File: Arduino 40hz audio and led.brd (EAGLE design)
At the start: 79.2 x 109.7 mm, 37 parts, among them IC1 LM7805, IC2 IRL-Z44N, IC3 LM741

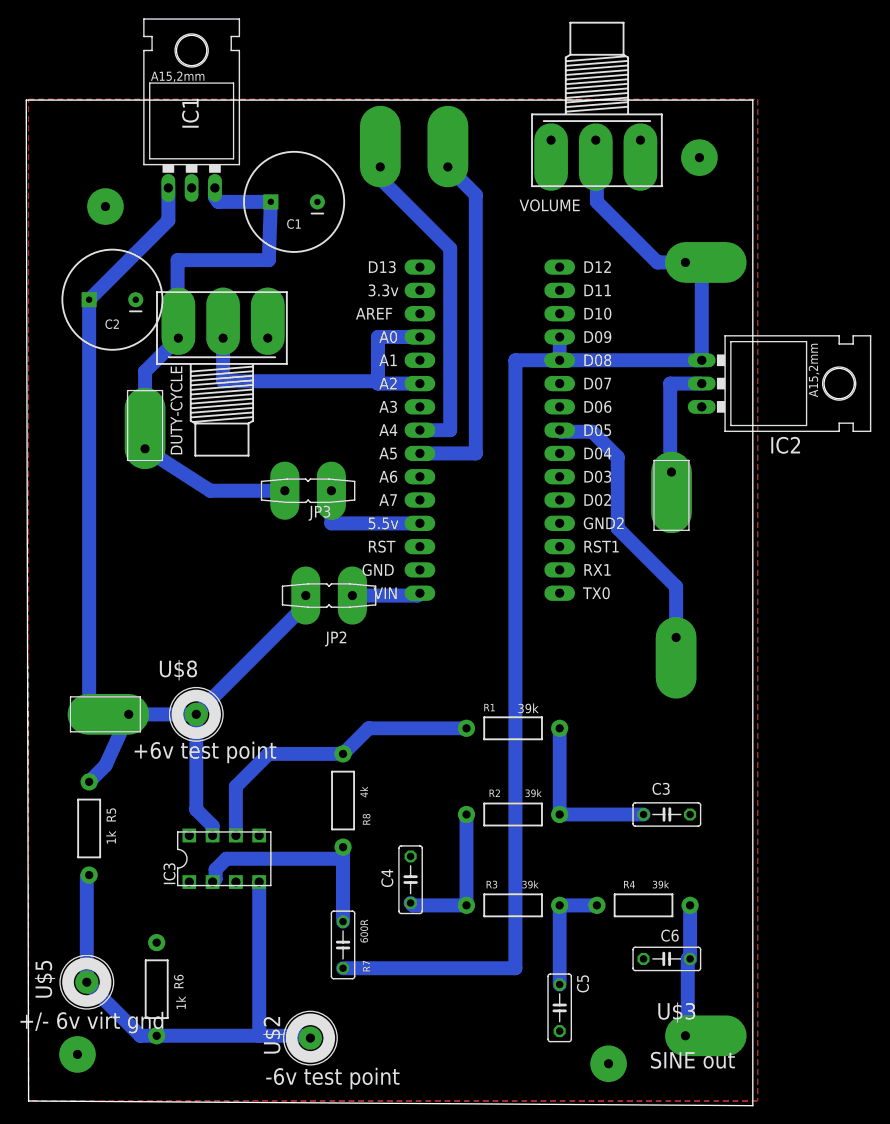
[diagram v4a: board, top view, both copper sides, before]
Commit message: Big update to this branch
Big update to this branch.  This branch I've completed the layout of the
board for single sided copper, where the parts are on top (no copper)
and the traces are on the bottom (copper layer).

I've worked quite a bit at setting trace width, spacing and part
spacing.
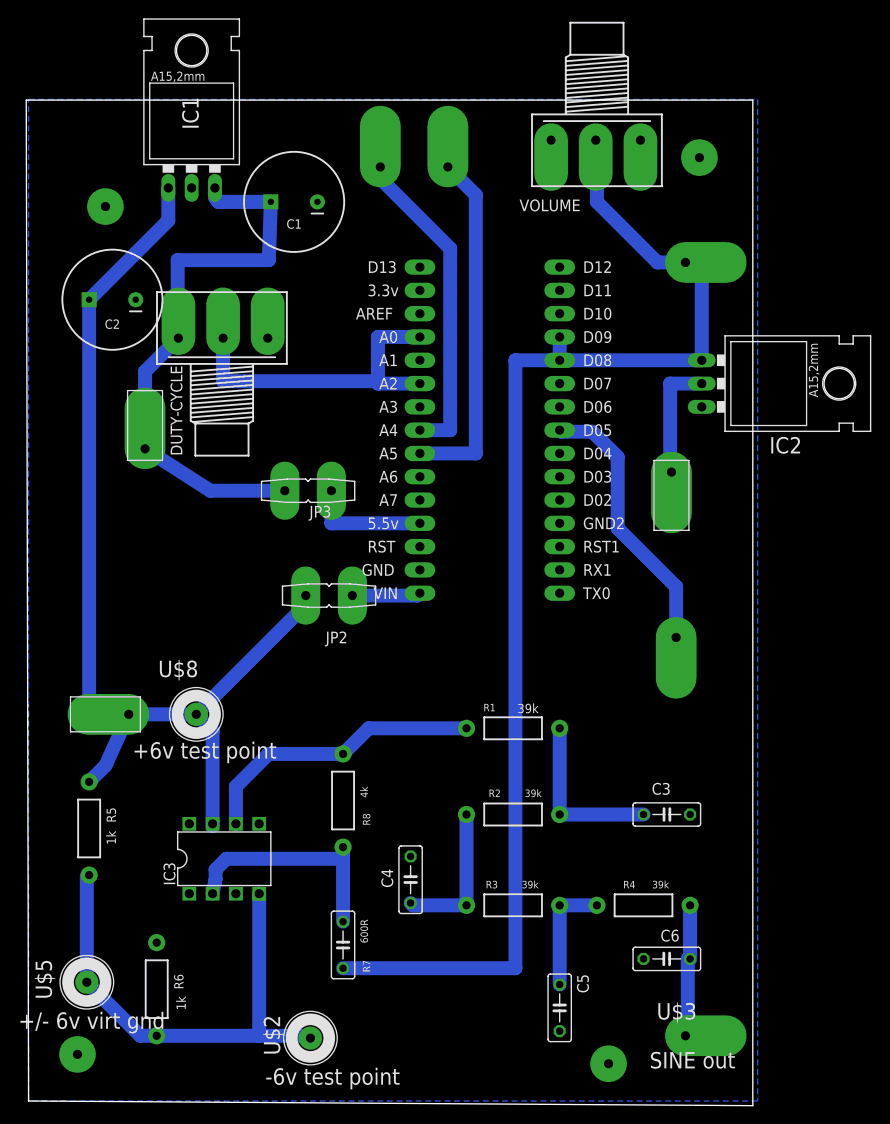
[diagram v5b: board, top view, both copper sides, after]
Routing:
- net N$13: track 33.1 -> 31.8 mm
- net N$12: track 55.5 -> 54.2 mm
- net N$10: track 24.0 -> 25.2 mm
- net +12V: track 113.2 -> 112.1 mm
- added copper zone on layer 16, net GND
- removed copper zone on layer 1, net GND
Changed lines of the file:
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@@
 <?xml version="1.0" encoding="utf-8"?>
 <!DOCTYPE eagle SYSTEM "eagle.dtd">
-<eagle version="9.2.2">
+<eagle version="9.4.2">
 <drawing>
 <settings>
@@
 <contactref element="C4" pad="2"/>
 <contactref element="C5" pad="2"/>
-<polygon width="0.9144" layer="1">
+<polygon width="0.9144" layer="16">
 <vertex x="-0.254" y="0.254"/>
 <vertex x="-0.254" y="109.474"/>
@@
 <wire x1="10.668" y1="42.418" x2="6.35" y2="42.418" width="1.524" layer="16"/>
 <wire x1="6.35" y1="42.418" x2="6.35" y2="87.63" width="1.524" layer="16"/>
-<wire x1="18.034" y1="32.02358125" x2="18.034" y2="42.418" width="1.524" layer="16"/>
-<wire x1="19.812" y1="29.21" x2="19.812" y2="30.24558125" width="1.524" layer="16"/>
-<wire x1="19.812" y1="30.24558125" x2="18.034" y2="32.02358125" width="1.524" layer="16"/>
+<wire x1="19.812" y1="40.64" x2="19.812" y2="30.48" width="1.524" layer="16"/>
+<wire x1="19.812" y1="40.64" x2="18.034" y2="42.418" width="1.524" layer="16"/>
+<wire x1="19.812" y1="30.48" x2="19.812" y2="30.24558125" width="1.524" layer="16"/>
 </signal>
 <signal name="+5V" class="2">
@@
 <wire x1="73.152" y1="78.486" x2="69.7088" y2="78.486" width="1.524" layer="16"/>
 <wire x1="69.7088" y1="78.486" x2="69.7088" y2="67.1972" width="1.524" layer="16"/>
+<wire x1="69.7088" y1="67.1972" x2="69.85" y2="68.834" width="0" layer="19" extent="16-16"/>
 <wire x1="27.686" y1="66.802" x2="69.7088" y2="67.1972" width="0" layer="19" extent="16-16"/>
 </signal>
@@
 <wire x1="20.955" y1="83.439" x2="20.955" y2="78.74" width="1.524" layer="16"/>
 <wire x1="20.955" y1="78.74" x2="37.846" y2="78.74" width="1.524" layer="16"/>
+<wire x1="42.164" y1="78.486" x2="42.418" y2="78.486" width="0" layer="19" extent="16-16"/>
 </signal>
 <signal name="N$2" class="2">
@@
 <wire x1="34.036" y1="38.1" x2="36.83" y2="40.894" width="1.524" layer="16"/>
 <wire x1="36.83" y1="40.894" x2="47.498" y2="40.894" width="1.524" layer="16"/>
-<wire x1="22.352" y1="29.21" x2="22.352" y2="34.544" width="1.524" layer="16"/>
+<wire x1="22.352" y1="30.48" x2="22.352" y2="34.544" width="1.524" layer="16"/>
 <wire x1="22.352" y1="34.544" x2="25.908" y2="38.1" width="1.524" layer="16"/>
 <wire x1="25.908" y1="38.1" x2="34.036" y2="38.1" width="1.524" layer="16"/>
@@
 <wire x1="71.628" y1="7.366" x2="71.628" y2="15.748" width="1.524" layer="16"/>
 <wire x1="71.628" y1="15.748" x2="71.882" y2="15.748" width="1.524" layer="16"/>
+<wire x1="71.628" y1="7.366" x2="71.374" y2="7.366" width="0" layer="19" extent="16-16"/>
 </signal>
 <signal name="N$8" class="2">
@@
 <wire x1="34.036" y1="27.94" x2="34.036" y2="26.67" width="1.524" layer="16"/>
 <wire x1="34.036" y1="26.67" x2="34.036" y2="19.812" width="1.524" layer="16"/>
-<wire x1="19.812" y1="24.13" x2="20.136" y2="24.454" width="1.524" layer="16"/>
+<wire x1="19.812" y1="22.86" x2="20.136" y2="24.454" width="1.524" layer="16"/>
 <wire x1="20.136" y1="24.454" x2="20.136" y2="25.48958125" width="1.524" layer="16"/>
 <wire x1="20.136" y1="25.48958125" x2="21.31641875" y2="26.67" width="1.524" layer="16"/>
@@
 <wire x1="13.716" y1="7.366" x2="11.938" y2="7.366" width="1.524" layer="16"/>
 <wire x1="11.938" y1="7.366" x2="6.096" y2="13.208" width="1.524" layer="16"/>
-<wire x1="24.892" y1="24.13" x2="24.892" y2="7.366" width="1.524" layer="16"/>
+<wire x1="24.892" y1="22.86" x2="24.892" y2="7.366" width="1.524" layer="16"/>
 </signal>
 </signals>
